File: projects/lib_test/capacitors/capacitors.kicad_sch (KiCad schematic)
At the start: 0 parts

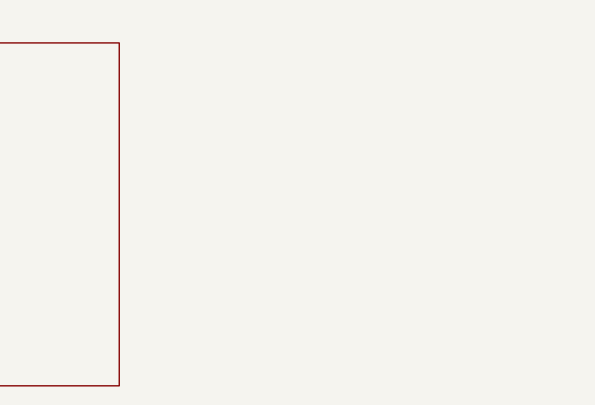
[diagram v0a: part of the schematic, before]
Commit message: updated capacitors test design
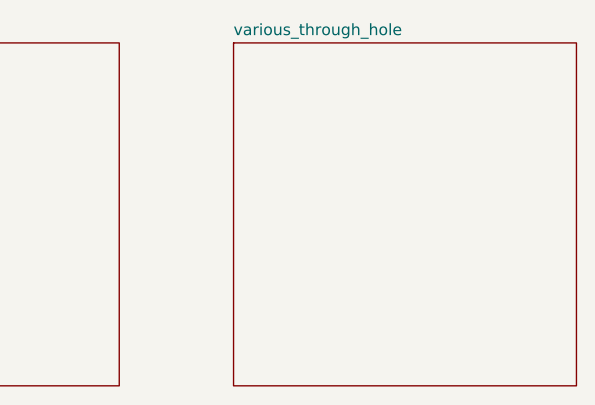
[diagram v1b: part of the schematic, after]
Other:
- added sheet various_through_hole (various_through_hole.kicad_sch)
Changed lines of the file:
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@@
+		)
+	)
+	(sheet
+		(at 127 25.4)
+		(size 38.1 38.1)
+		(exclude_from_sim no)
+		(in_bom yes)
+		(on_board yes)
+		(dnp no)
+		(fields_autoplaced yes)
+		(stroke
+			(width 0.1524)
+			(type solid)
+		)
+		(fill
+			(color 0 0 0 0.0000)
+		)
+		(property "Sheetname" "various_through_hole"
+			(at 127 24.6884 0)
+			(effects
+				(font
+					(size 1.27 1.27)
+				)
+				(justify left bottom)
+			)
+		)
+		(property "Sheetfile" "various_through_hole.kicad_sch"
+			(at 127 64.0846 0)
+			(effects
+				(font
+					(size 1.27 1.27)
+				)
+				(justify left top)
+				(hide yes)
+			)
+		)
+		(instances
+			(project "capacitors"
+				(path "/e63e39d7-6ac0-4ffd-8aa3-1841a4541b55"
+					(page "4")
+				)
+			)
 		)
 	)

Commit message: updated test project
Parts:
- added C1001: 1p0, lily_footprints:cap_0805, symbol lily_symbols:cap_1p0_50V_5%_C0G_0805
- added C1002: 1p2, lily_footprints:cap_0805, symbol lily_symbols:cap_1p2_50V_5%_C0G_0805
- added C1003: 1p5, lily_footprints:cap_0805, symbol lily_symbols:cap_1p5_50V_5%_C0G_0805
- added C1004: 1p8, lily_footprints:cap_0805, symbol lily_symbols:cap_1p8_50V_5%_C0G_0805
- added C1005: 2p2, lily_footprints:cap_0805, symbol lily_symbols:cap_2p2_50V_5%_C0G_0805
- added C1006: 2p7, lily_footprints:cap_0805, symbol lily_symbols:cap_2p7_50V_5%_C0G_0805
- added C1007: 3p3, lily_footprints:cap_0805, symbol lily_symbols:cap_3p3_50V_5%_C0G_0805
- added C1008: 3p9, lily_footprints:cap_0805, symbol lily_symbols:cap_3p9_50V_5%_C0G_0805
- added C1009: 4p7, lily_footprints:cap_0805, symbol lily_symbols:cap_4p7_50V_5%_C0G_0805
- added C1010: 5p6, lily_footprints:cap_0805, symbol lily_symbols:cap_5p6_50V_5%_C0G_0805
- added C1011: 6p8, lily_footprints:cap_0805, symbol lily_symbols:cap_6p8_50V_5%_C0G_0805
- added C1012: 8p2, lily_footprints:cap_0805, symbol lily_symbols:cap_8p2_50V_5%_C0G_0805
- added C1013: 10u, lily_footprints:cap_0805, symbol lily_symbols:cap_10u_25V_10%_X5R_0805
- added C1014: 22u, lily_footprints:cap_0805, symbol lily_symbols:cap_22u_16V_10%_X5R_0805
- added C1015: 10p, lily_footprints:cap_0805, symbol lily_symbols:cap_10p_50V_5%_C0G_0805
- added C1016: 12p, lily_footprints:cap_0805, symbol lily_symbols:cap_12p_50V_5%_C0G_0805
- added C1017: 15p, lily_footprints:cap_0805, symbol lily_symbols:cap_15p_50V_5%_C0G_0805
- added C1018: 18p, lily_footprints:cap_0805, symbol lily_symbols:cap_18p_50V_5%_C0G_0805
- added C1019: 22p, lily_footprints:cap_0805, symbol lily_symbols:cap_22p_50V_5%_C0G_0805
- added C1020: 27p, lily_footprints:cap_0805, symbol lily_symbols:cap_27p_50V_5%_C0G_0805
- added C1021: 33p, lily_footprints:cap_0805, symbol lily_symbols:cap_33p_50V_5%_C0G_0805
- added C1022: 39p, lily_footprints:cap_0805, symbol lily_symbols:cap_39p_50V_5%_C0G_0805
- added C1023: 47p, lily_footprints:cap_0805, symbol lily_symbols:cap_47p_50V_5%_C0G_0805
- added C1024: 56p, lily_footprints:cap_0805, symbol lily_symbols:cap_56p_50V_5%_C0G_0805
- added C1025: 68p, lily_footprints:cap_0805, symbol lily_symbols:cap_68p_50V_5%_C0G_0805
- added C1026: 82p, lily_footprints:cap_0805, symbol lily_symbols:cap_82p_50V_5%_C0G_0805
- added C1027: 100p, lily_footprints:cap_0805, symbol lily_symbols:cap_100p_50V_5%_C0G_0805
- added C1028: 120p, lily_footprints:cap_0805, symbol lily_symbols:cap_120p_50V_5%_C0G_0805
- added C1029: 150p, lily_footprints:cap_0805, symbol lily_symbols:cap_150p_50V_5%_C0G_0805
- added C1030: 180p, lily_footprints:cap_0805, symbol lily_symbols:cap_180p_50V_5%_C0G_0805
- added C1031: 220p, lily_footprints:cap_0805, symbol lily_symbols:cap_220p_50V_5%_C0G_0805
- added C1032: 270p, lily_footprints:cap_0805, symbol lily_symbols:cap_270p_50V_5%_C0G_0805
- added C1033: 330p, lily_footprints:cap_0805, symbol lily_symbols:cap_330p_50V_5%_C0G_0805
- added C1034: 390p, lily_footprints:cap_0805, symbol lily_symbols:cap_390p_50V_5%_C0G_0805
- added C1035: 470p, lily_footprints:cap_0805, symbol lily_symbols:cap_470p_50V_5%_C0G_0805
- added C1036: 560p, lily_footprints:cap_0805, symbol lily_symbols:cap_560p_50V_5%_C0G_0805
- added C1037: 680p, lily_footprints:cap_0805, symbol lily_symbols:cap_680p_50V_5%_C0G_0805
- added C1038: 820p, lily_footprints:cap_0805, symbol lily_symbols:cap_820p_50V_5%_C0G_0805
- added C1039: 1n0, lily_footprints:cap_0805, symbol lily_symbols:cap_1n0_50V_10%_X7R_0805
- added C1040: 1n2, lily_footprints:cap_0805, symbol lily_symbols:cap_1n2_50V_10%_X7R_0805
- added C1041: 1n5, lily_footprints:cap_0805, symbol lily_symbols:cap_1n5_50V_10%_X7R_0805
- added C1042: 1n8, lily_footprints:cap_0805, symbol lily_symbols:cap_1n8_50V_10%_X7R_0805
- added C1043: 2n2, lily_footprints:cap_0805, symbol lily_symbols:cap_2n2_50V_10%_X7R_0805
- added C1044: 2n7, lily_footprints:cap_0805, symbol lily_symbols:cap_2n7_50V_10%_X7R_0805
- added C1045: 3n3, lily_footprints:cap_0805, symbol lily_symbols:cap_3n3_50V_10%_X7R_0805
- added C1046: 3n9, lily_footprints:cap_0805, symbol lily_symbols:cap_3n9_50V_10%_X7R_0805
- added C1047: 4n7, lily_footprints:cap_0805, symbol lily_symbols:cap_4n7_50V_10%_X7R_0805
- added C1048: 5n6, lily_footprints:cap_0805, symbol lily_symbols:cap_5n6_50V_10%_X7R_0805
- added C1049: 6n8, lily_footprints:cap_0805, symbol lily_symbols:cap_6n8_50V_10%_X7R_0805
- added C1050: 8n2, lily_footprints:cap_0805, symbol lily_symbols:cap_8n2_50V_10%_X7R_0805
- added C1051: 10n, lily_footprints:cap_0805, symbol lily_symbols:cap_10n_50V_10%_X7R_0805
- added C1052: 12n, lily_footprints:cap_0805, symbol lily_symbols:cap_12n_50V_10%_X7R_0805
- added C1053: 15n, lily_footprints:cap_0805, symbol lily_symbols:cap_15n_50V_10%_X7R_0805
- added C1054: 18n, lily_footprints:cap_0805, symbol lily_symbols:cap_18n_50V_10%_X7R_0805
- added C1055: 22n, lily_footprints:cap_0805, symbol lily_symbols:cap_22n_50V_10%_X7R_0805
- added C1056: 27n, lily_footprints:cap_0805, symbol lily_symbols:cap_27n_50V_10%_X7R_0805
- added C1057: 33n, lily_footprints:cap_0805, symbol lily_symbols:cap_33n_50V_10%_X7R_0805
- added C1058: 39n, lily_footprints:cap_0805, symbol lily_symbols:cap_39n_50V_10%_X7R_0805
- added C1059: 47n, lily_footprints:cap_0805, symbol lily_symbols:cap_47n_50V_10%_X7R_0805
- added C1060: 56n, lily_footprints:cap_0805, symbol lily_symbols:cap_56n_50V_10%_X7R_0805
- added C1061: 68n, lily_footprints:cap_0805, symbol lily_symbols:cap_68n_50V_10%_X7R_0805
- added C1062: 82n, lily_footprints:cap_0805, symbol lily_symbols:cap_82n_50V_10%_X7R_0805
- added C1063: 100n, lily_footprints:cap_0805, symbol lily_symbols:cap_100n_50V_10%_X7R_0805
- added C1064: 120n, lily_footprints:cap_0805, symbol lily_symbols:cap_120n_50V_10%_X7R_0805
- added C1065: 150n, lily_footprints:cap_0805, symbol lily_symbols:cap_150n_50V_10%_X7R_0805
- added C1066: 180n, lily_footprints:cap_0805, symbol lily_symbols:cap_180n_50V_10%_X7R_0805
- added C1067: 220n, lily_footprints:cap_0805, symbol lily_symbols:cap_220n_50V_10%_X7R_0805
- added C1068: 270n, lily_footprints:cap_0805, symbol lily_symbols:cap_270n_50V_10%_X7R_0805
- added C1069: 330n, lily_footprints:cap_0805, symbol lily_symbols:cap_330n_50V_10%_X7R_0805
- added C1070: 390n, lily_footprints:cap_0805, symbol lily_symbols:cap_390n_50V_10%_X7R_0805
- added C1071: 470n, lily_footprints:cap_0805, symbol lily_symbols:cap_470n_50V_10%_X7R_0805
- added C1072: 560n, lily_footprints:cap_0805, symbol lily_symbols:cap_560n_50V_10%_X7R_0805
- added C1073: 680n, lily_footprints:cap_0805, symbol lily_symbols:cap_680n_50V_10%_X7R_0805
- added C1074: 820n, lily_footprints:cap_0805, symbol lily_symbols:cap_820n_50V_10%_X7R_0805
- added C1075: 47u, lily_footprints:cap_1210, symbol lily_symbols:cap_47u_16V_10%_X5R_1210
- added C1076: 20p, lily_footprints:cap_trimmer_jz_series, symbol lily_symbols:cap_trimmer_20p_100V_500ppm_JZ
- added C1077: 15m, lily_footprints:cap_elec_rad_35x52mm_th, symbol lily_symbols:cap_elec_15m_50V_20%_rad_35x52mm_th
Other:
- removed sheet e12_0805
- removed sheet various_smd
- removed sheet various_through_hole
- note added: "0805 (E12)"
- note added: "1210"
- note added: "THROUGH HOLE"
- note added: "VARIABLE"

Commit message: updated lib test
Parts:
- added C1078: 1u0, lily_footprints:cap_0805, symbol lily_symbols:cap_1u0_50V_10%_X7R_0805
- added C1079: 4u7, lily_footprints:cap_0805, symbol lily_symbols:cap_4u7_25V_10%_X5R_0805
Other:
- moved on the sheet: C1013, C1014

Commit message: updated capacitors test project
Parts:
- renumbered C1078 to C1013, C1079 to C1014, C1013 to C1027, C1014 to C1028, C1027 to C1029, C1028 to C1030, C1029 to C1031, C1030 to C1032, C1031 to C1033, C1032 to C1034, C1033 to C1035, C1034 to C1036, C1035 to C1037, C1036 to C1038, C1037 to C1039, C1038 to C1040, C1039 to C1041, C1040 to C1042, C1041 to C1043, C1042 to C1044, C1043 to C1045, C1044 to C1046, C1045 to C1047, C1046 to C1048, C1047 to C1049, C1048 to C1050, C1049 to C1051, C1050 to C1052, C1051 to C1053, C1052 to C1054, C1053 to C1055, C1054 to C1056, C1055 to C1057, C1056 to C1058, C1057 to C1059, C1058 to C1060, C1059 to C1061, C1060 to C1062, C1061 to C1063, C1062 to C1064, C1063 to C1065, C1064 to C1066, C1065 to C1067, C1066 to C1068, C1067 to C1069, C1068 to C1070, C1069 to C1071, C1070 to C1072, C1071 to C1073, C1072 to C1074, C1073 to C1075, C1074 to C1076, C1075 to C1077, C1076 to C1078, C1077 to C1079
